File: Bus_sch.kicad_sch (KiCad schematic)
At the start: 9 parts, among them J15 Conn_01x03_Male, J16 Conn_01x20_Male, J17 Conn_01x16_Male, U23 74LS244, U24 74LS373, U25 74LS373, U26 74LS373, U27 74LS245, U28 74LS245

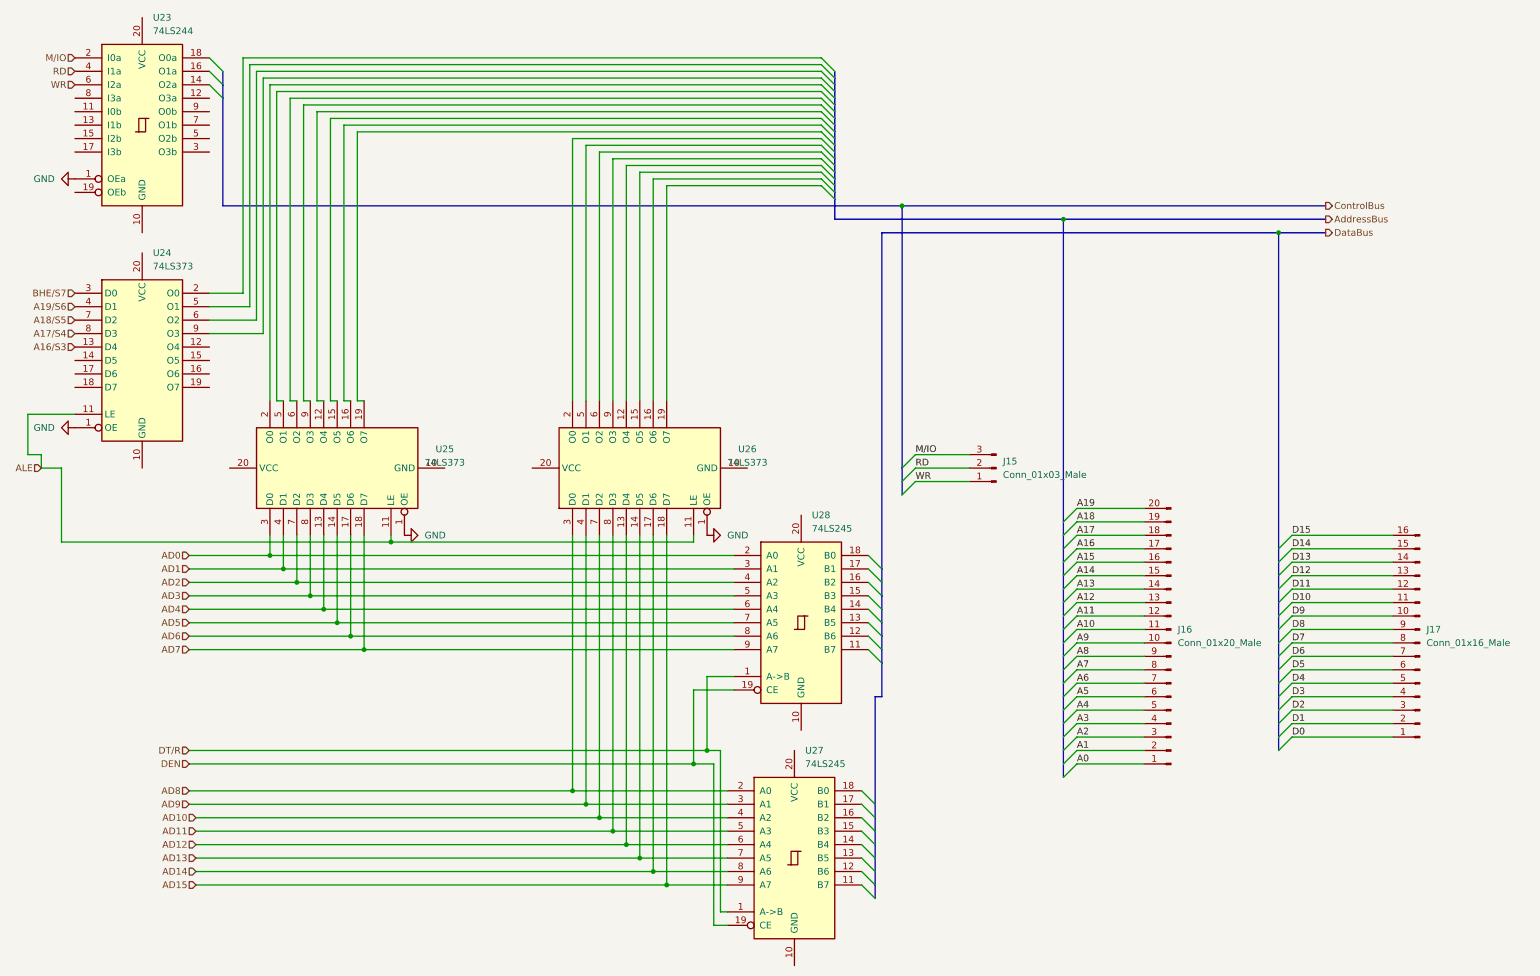
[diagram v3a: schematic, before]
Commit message: Added power and ground to chips
Added power and ground to chips as well as checked and added all labels for pins off of busses
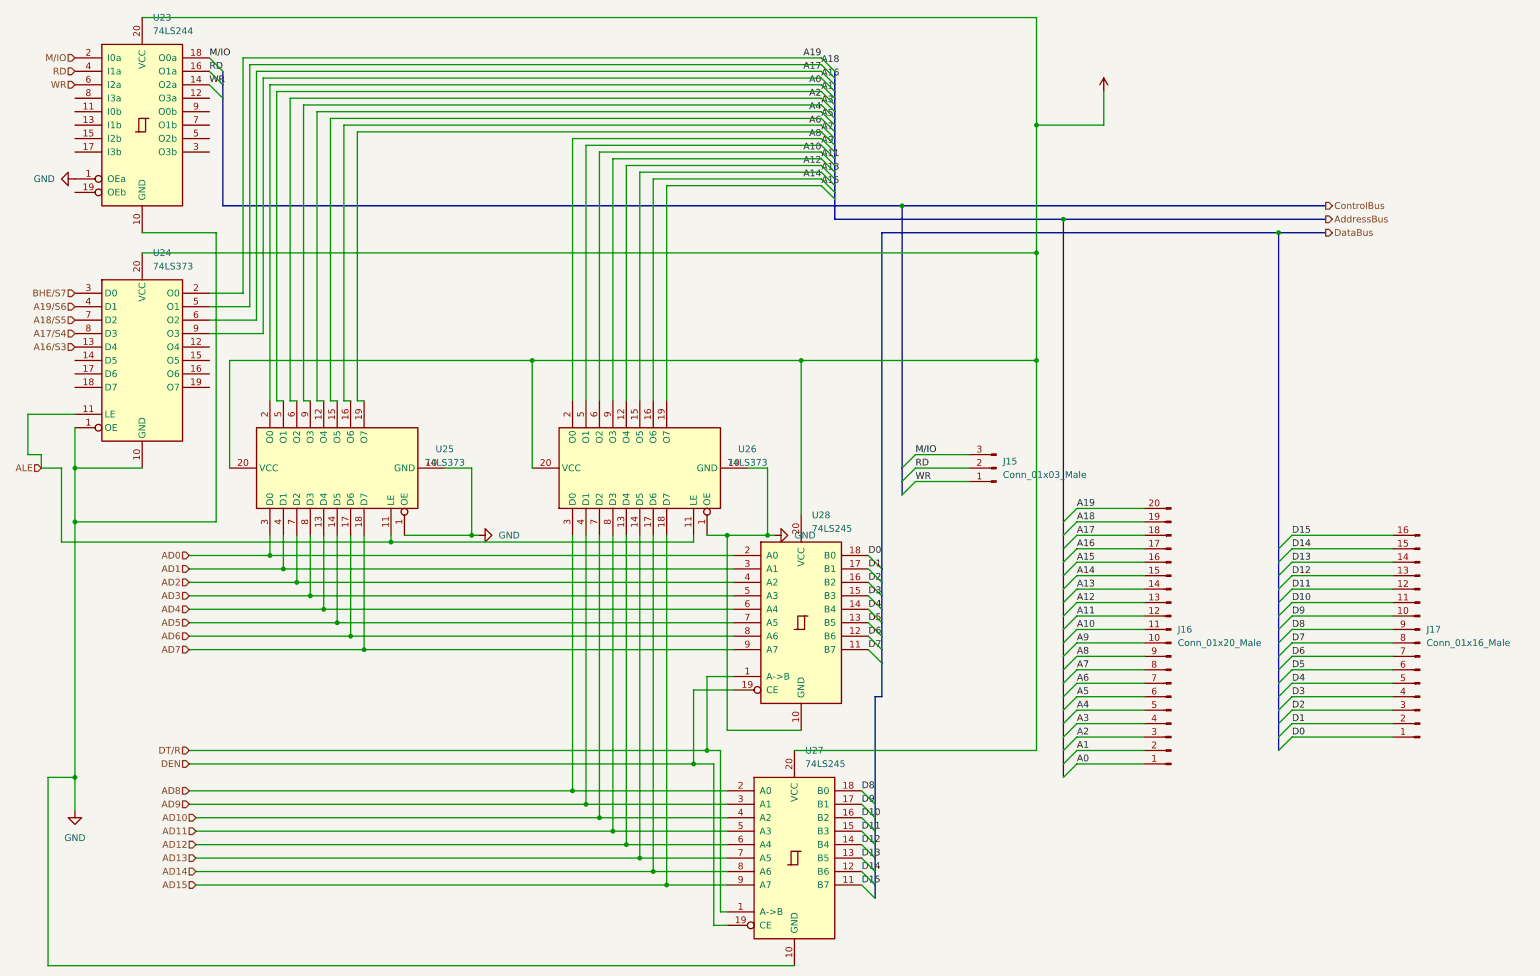
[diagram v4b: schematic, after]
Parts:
- J15, J16, J17: footprint (none) -> Connector:FanPinHeader_1x03_P2.54mm_Vertical
- U23, U24, U25, U26, U27, U28: footprint (none) -> Package_DIP:DIP-20_W7.62mm
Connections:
- net A0: now also U25.2 (O0)
- net A1: now also U25.5 (O1)
- net A10: now also U26.6 (O2)
- net A11: now also U26.9 (O3)
- net A12: now also U26.12 (O4)
- net A13: now also U26.15 (O5)
- net A14: now also U26.16 (O6)
- net A15: now also U26.19 (O7)
- net A16: now also U24.9 (O3)
- net A17: now also U24.6 (O2)
- net A18: now also U24.5 (O1)
- net A19: now also U24.2 (O0)
- net A2: now also U25.6 (O2)
- net A3: now also U25.9 (O3)
- net A4: now also U25.12 (O4)
- net A5: now also U25.15 (O5)
- net A6: now also U25.16 (O6)
- net A7: now also U25.19 (O7)
- net A8: now also U26.2 (O0)
- net A9: now also U26.5 (O1)
- net D0: now also U28.18 (B0)
- net D1: now also U28.17 (B1)
- net D10: now also U27.16 (B2)
- net D11: now also U27.15 (B3)
- net D12: now also U27.14 (B4)
- net D13: now also U27.13 (B5)
- net D14: now also U27.12 (B6)
- net D15: now also U27.11 (B7)
- net D2: now also U28.16 (B2)
- net D3: now also U28.15 (B3)
- net D4: now also U28.14 (B4)
- net D5: now also U28.13 (B5)
- net D6: now also U28.12 (B6)
- net D7: now also U28.11 (B7)
- net D8: now also U27.18 (B0)
- net D9: now also U27.17 (B1)
- net GND: now also U23.10 (GND), U24.10 (GND), U25.10 (GND), U26.10 (GND), U27.10 (GND), U28.10 (GND)
- net M/IO: now also U23.18 (O0a)
- net RD: now also U23.16 (O1a)
- net WR: now also U23.14 (O2a)
- net +5V: now reaches U24.20 (VCC)
- net +5V: now also U23.20 (VCC), U25.20 (VCC), U26.20 (VCC), U27.20 (VCC), U28.20 (VCC)

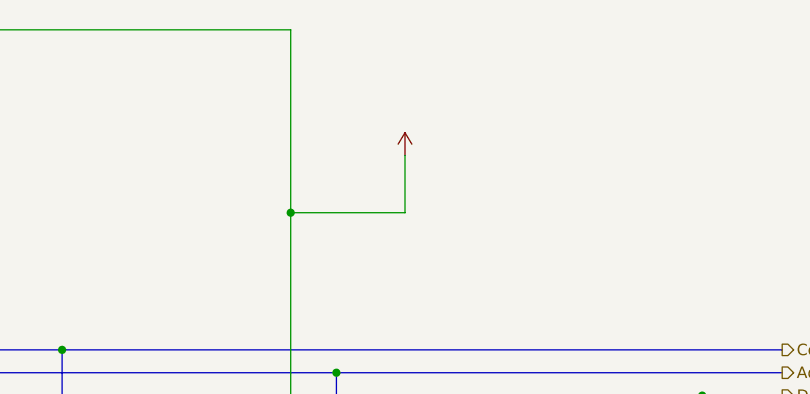
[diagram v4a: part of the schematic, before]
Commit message: Enabled inputs on the max235
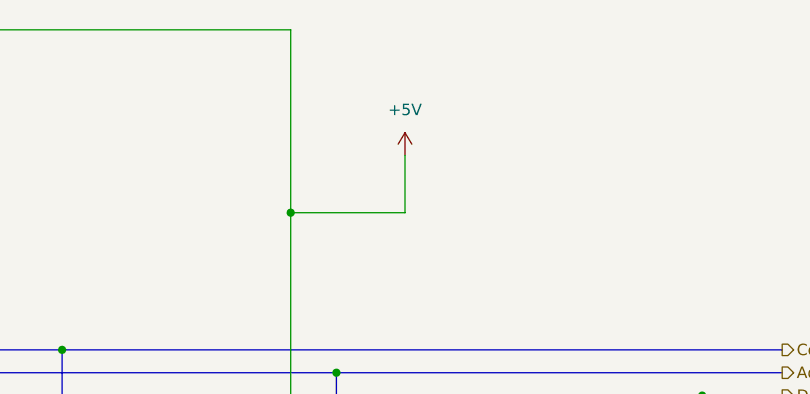
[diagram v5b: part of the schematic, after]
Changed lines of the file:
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@@
       (effects (font (size 1.27 1.27)) hide)
     )
-    (property "Value" "" (id 1) (at 218.44 19.05 0))
+    (property "Value" "+5V" (id 1) (at 218.44 19.05 0))
     (property "Footprint" "" (id 2) (at 218.44 24.13 0)
       (effects (font (size 1.27 1.27)) hide)

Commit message: Updated PCB
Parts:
- J15: value Conn_01x03_Male -> (none); footprint Connector:FanPinHeader_1x03_P2.54mm_Vertical -> (none)
- J16: value Conn_01x20_Male -> (none); footprint Connector:FanPinHeader_1x03_P2.54mm_Vertical -> (none)
- J17: value Conn_01x16_Male -> (none); footprint Connector:FanPinHeader_1x03_P2.54mm_Vertical -> (none)
- U23: value 74LS244 -> (none); footprint Package_DIP:DIP-20_W7.62mm -> (none)
- U24, U25, U26: value 74LS373 -> (none); footprint Package_DIP:DIP-20_W7.62mm -> (none)
- U27, U28: value 74LS245 -> (none); footprint Package_DIP:DIP-20_W7.62mm -> (none)
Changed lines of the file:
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@@
       (effects (font (size 1.27 1.27)) (justify left))
     )
-    (property "Value" "74LS373" (id 1) (at 38.8494 57.15 0)
-      (effects (font (size 1.27 1.27)) (justify left))
-    )
-    (property "Footprint" "Package_DIP:DIP-20_W7.62mm" (id 2) (at 36.83 74.93 0)
+    (property "Value" "" (id 1) (at 38.8494 57.15 0)
+      (effects (font (size 1.27 1.27)) (justify left))
+    )
+    (property "Footprint" "" (id 2) (at 36.83 74.93 0)
       (effects (font (size 1.27 1.27)) hide)
     )
@@
     (in_bom yes) (on_board yes) (fields_autoplaced)
     (property "Reference" "U26" (id 0) (at 151.13 91.6686 90))
-    (property "Value" "74LS373" (id 1) (at 151.13 94.2086 90))
-    (property "Footprint" "Package_DIP:DIP-20_W7.62mm" (id 2) (at 130.81 95.25 0)
+    (property "Value" "" (id 1) (at 151.13 94.2086 90))
+    (property "Footprint" "" (id 2) (at 130.81 95.25 0)
       (effects (font (size 1.27 1.27)) hide)
     )
@@
       (effects (font (size 1.27 1.27)) (justify left))
     )
-    (property "Value" "74LS245" (id 1) (at 163.3094 106.68 0)
-      (effects (font (size 1.27 1.27)) (justify left))
-    )
-    (property "Footprint" "Package_DIP:DIP-20_W7.62mm" (id 2) (at 161.29 124.46 0)
+    (property "Value" "" (id 1) (at 163.3094 106.68 0)
+      (effects (font (size 1.27 1.27)) (justify left))
+    )
+    (property "Footprint" "" (id 2) (at 161.29 124.46 0)
       (effects (font (size 1.27 1.27)) hide)
     )
@@
       (effects (font (size 1.27 1.27)) (justify right))
     )
-    (property "Value" "Conn_01x16_Male" (id 1) (at 279.4 128.2699 0)
-      (effects (font (size 1.27 1.27)) (justify right))
-    )
-    (property "Footprint" "Connector:FanPinHeader_1x03_P2.54mm_Vertical" (id 2) (at 278.13 128.27 0)
+    (property "Value" "" (id 1) (at 279.4 128.2699 0)
+      (effects (font (size 1.27 1.27)) (justify right))
+    )
+    (property "Footprint" "" (id 2) (at 278.13 128.27 0)
       (effects (font (size 1.27 1.27)) hide)
     )
@@
   (symbol (lib_id "power:+5V") (at 218.44 24.13 0) (unit 1)
     (in_bom yes) (on_board yes) (fields_autoplaced)
-    (property "Reference" "#PWR?" (id 0) (at 218.44 27.94 0)
+    (property "Reference" "#PWR0131" (id 0) (at 218.44 27.94 0)
       (effects (font (size 1.27 1.27)) hide)
     )
@@
       (effects (font (size 1.27 1.27)) (justify right))
     )
-    (property "Value" "Conn_01x20_Male" (id 1) (at 232.41 128.2699 0)
-      (effects (font (size 1.27 1.27)) (justify right))
-    )
-    (property "Footprint" "Connector:FanPinHeader_1x03_P2.54mm_Vertical" (id 2) (at 231.14 128.27 0)
+    (property "Value" "" (id 1) (at 232.41 128.2699 0)
+      (effects (font (size 1.27 1.27)) (justify right))
+    )
+    (property "Footprint" "" (id 2) (at 231.14 128.27 0)
       (effects (font (size 1.27 1.27)) hide)
     )
@@
     (in_bom yes) (on_board yes) (fields_autoplaced)
     (property "Reference" "U25" (id 0) (at 93.98 91.6686 90))
-    (property "Value" "74LS373" (id 1) (at 93.98 94.2086 90))
-    (property "Footprint" "Package_DIP:DIP-20_W7.62mm" (id 2) (at 73.66 95.25 0)
+    (property "Value" "" (id 1) (at 93.98 94.2086 90))
+    (property "Footprint" "" (id 2) (at 73.66 95.25 0)
       (effects (font (size 1.27 1.27)) hide)
     )
@@
       (effects (font (size 1.27 1.27)) (justify left))
     )
-    (property "Value" "74LS245" (id 1) (at 162.0394 151.13 0)
-      (effects (font (size 1.27 1.27)) (justify left))
-    )
-    (property "Footprint" "Package_DIP:DIP-20_W7.62mm" (id 2) (at 160.02 168.91 0)
+    (property "Value" "" (id 1) (at 162.0394 151.13 0)
+      (effects (font (size 1.27 1.27)) (justify left))
+    )
+    (property "Footprint" "" (id 2) (at 160.02 168.91 0)
       (effects (font (size 1.27 1.27)) hide)
     )
@@
       (effects (font (size 1.27 1.27)) (justify right))
     )
-    (property "Value" "Conn_01x03_Male" (id 1) (at 199.39 96.5199 0)
-      (effects (font (size 1.27 1.27)) (justify right))
-    )
-    (property "Footprint" "Connector:FanPinHeader_1x03_P2.54mm_Vertical" (id 2) (at 198.12 95.25 0)
+    (property "Value" "" (id 1) (at 199.39 96.5199 0)
+      (effects (font (size 1.27 1.27)) (justify right))
+    )
+    (property "Footprint" "" (id 2) (at 198.12 95.25 0)
       (effects (font (size 1.27 1.27)) hide)
     )
@@
       (effects (font (size 1.27 1.27)) (justify left))
     )
-    (property "Value" "74LS244" (id 1) (at 38.8494 12.7 0)
-      (effects (font (size 1.27 1.27)) (justify left))
-    )
-    (property "Footprint" "Package_DIP:DIP-20_W7.62mm" (id 2) (at 36.83 30.48 0)
-      (effects (font (size 1.27 1.27)) hide)
-    )
+    (property "Value" "" (id 1) (at 38.8494 12.7 0)
+      (effects (font (size 1.27 1.27)) (justify left))
+    )
+    (property "Footprint" "" (id 2) (at 36.83 30.48 0)
+      (effects (font (size 1.27 1.27)) hide)
+    )

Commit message: PCB wiring
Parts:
- J15: value (none) -> Conn_01x03_Male; footprint (none) -> Connector:FanPinHeader_1x03_P2.54mm_Vertical
- J16: value (none) -> Conn_01x20_Male; footprint (none) -> Connector:FanPinHeader_1x03_P2.54mm_Vertical
- J17: value (none) -> Conn_01x16_Male; footprint (none) -> Connector:FanPinHeader_1x03_P2.54mm_Vertical
- U23: value (none) -> 74LS244; footprint (none) -> Package_DIP:DIP-20_W7.62mm
- U24, U25, U26: value (none) -> 74LS373; footprint (none) -> Package_DIP:DIP-20_W7.62mm
- U27, U28: value (none) -> 74LS245; footprint (none) -> Package_DIP:DIP-20_W7.62mm
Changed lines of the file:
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@@
       (effects (font (size 1.27 1.27)) (justify left))
     )
-    (property "Value" "" (id 1) (at 38.8494 57.15 0)
-      (effects (font (size 1.27 1.27)) (justify left))
-    )
-    (property "Footprint" "" (id 2) (at 36.83 74.93 0)
+    (property "Value" "74LS373" (id 1) (at 38.8494 57.15 0)
+      (effects (font (size 1.27 1.27)) (justify left))
+    )
+    (property "Footprint" "Package_DIP:DIP-20_W7.62mm" (id 2) (at 36.83 74.93 0)
       (effects (font (size 1.27 1.27)) hide)
     )
@@
     (in_bom yes) (on_board yes) (fields_autoplaced)
     (property "Reference" "U26" (id 0) (at 151.13 91.6686 90))
-    (property "Value" "" (id 1) (at 151.13 94.2086 90))
-    (property "Footprint" "" (id 2) (at 130.81 95.25 0)
+    (property "Value" "74LS373" (id 1) (at 151.13 94.2086 90))
+    (property "Footprint" "Package_DIP:DIP-20_W7.62mm" (id 2) (at 130.81 95.25 0)
       (effects (font (size 1.27 1.27)) hide)
     )
@@
       (effects (font (size 1.27 1.27)) (justify left))
     )
-    (property "Value" "" (id 1) (at 163.3094 106.68 0)
-      (effects (font (size 1.27 1.27)) (justify left))
-    )
-    (property "Footprint" "" (id 2) (at 161.29 124.46 0)
+    (property "Value" "74LS245" (id 1) (at 163.3094 106.68 0)
+      (effects (font (size 1.27 1.27)) (justify left))
+    )
+    (property "Footprint" "Package_DIP:DIP-20_W7.62mm" (id 2) (at 161.29 124.46 0)
       (effects (font (size 1.27 1.27)) hide)
     )
@@
       (effects (font (size 1.27 1.27)) (justify right))
     )
-    (property "Value" "" (id 1) (at 279.4 128.2699 0)
-      (effects (font (size 1.27 1.27)) (justify right))
-    )
-    (property "Footprint" "" (id 2) (at 278.13 128.27 0)
+    (property "Value" "Conn_01x16_Male" (id 1) (at 279.4 128.2699 0)
+      (effects (font (size 1.27 1.27)) (justify right))
+    )
+    (property "Footprint" "Connector:FanPinHeader_1x03_P2.54mm_Vertical" (id 2) (at 278.13 128.27 0)
       (effects (font (size 1.27 1.27)) hide)
     )
@@
       (effects (font (size 1.27 1.27)) (justify right))
     )
-    (property "Value" "" (id 1) (at 232.41 128.2699 0)
-      (effects (font (size 1.27 1.27)) (justify right))
-    )
-    (property "Footprint" "" (id 2) (at 231.14 128.27 0)
+    (property "Value" "Conn_01x20_Male" (id 1) (at 232.41 128.2699 0)
+      (effects (font (size 1.27 1.27)) (justify right))
+    )
+    (property "Footprint" "Connector:FanPinHeader_1x03_P2.54mm_Vertical" (id 2) (at 231.14 128.27 0)
       (effects (font (size 1.27 1.27)) hide)
     )
@@
     (in_bom yes) (on_board yes) (fields_autoplaced)
     (property "Reference" "U25" (id 0) (at 93.98 91.6686 90))
-    (property "Value" "" (id 1) (at 93.98 94.2086 90))
-    (property "Footprint" "" (id 2) (at 73.66 95.25 0)
+    (property "Value" "74LS373" (id 1) (at 93.98 94.2086 90))
+    (property "Footprint" "Package_DIP:DIP-20_W7.62mm" (id 2) (at 73.66 95.25 0)
       (effects (font (size 1.27 1.27)) hide)
     )
@@
       (effects (font (size 1.27 1.27)) (justify left))
     )
-    (property "Value" "" (id 1) (at 162.0394 151.13 0)
-      (effects (font (size 1.27 1.27)) (justify left))
-    )
-    (property "Footprint" "" (id 2) (at 160.02 168.91 0)
+    (property "Value" "74LS245" (id 1) (at 162.0394 151.13 0)
+      (effects (font (size 1.27 1.27)) (justify left))
+    )
+    (property "Footprint" "Package_DIP:DIP-20_W7.62mm" (id 2) (at 160.02 168.91 0)
       (effects (font (size 1.27 1.27)) hide)
     )
@@
       (effects (font (size 1.27 1.27)) (justify right))
     )
-    (property "Value" "" (id 1) (at 199.39 96.5199 0)
-      (effects (font (size 1.27 1.27)) (justify right))
-    )
-    (property "Footprint" "" (id 2) (at 198.12 95.25 0)
+    (property "Value" "Conn_01x03_Male" (id 1) (at 199.39 96.5199 0)
+      (effects (font (size 1.27 1.27)) (justify right))
+    )
+    (property "Footprint" "Connector:FanPinHeader_1x03_P2.54mm_Vertical" (id 2) (at 198.12 95.25 0)
       (effects (font (size 1.27 1.27)) hide)
     )
@@
       (effects (font (size 1.27 1.27)) (justify left))
     )
-    (property "Value" "" (id 1) (at 38.8494 12.7 0)
-      (effects (font (size 1.27 1.27)) (justify left))
-    )
-    (property "Footprint" "" (id 2) (at 36.83 30.48 0)
-      (effects (font (size 1.27 1.27)) hide)
-    )
+    (property "Value" "74LS244" (id 1) (at 38.8494 12.7 0)
+      (effects (font (size 1.27 1.27)) (justify left))
+    )
+    (property "Footprint" "Package_DIP:DIP-20_W7.62mm" (id 2) (at 36.83 30.48 0)
+      (effects (font (size 1.27 1.27)) hide)
+    )

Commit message: pcb wiring
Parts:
- J16, J17: footprint Connector:FanPinHeader_1x03_P2.54mm_Vertical -> (none)
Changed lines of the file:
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@@
       (effects (font (size 1.27 1.27)) (justify right))
     )
-    (property "Footprint" "Connector:FanPinHeader_1x03_P2.54mm_Vertical" (id 2) (at 278.13 128.27 0)
+    (property "Footprint" "" (id 2) (at 278.13 128.27 0)
       (effects (font (size 1.27 1.27)) hide)
     )
@@
       (effects (font (size 1.27 1.27)) (justify right))
     )
-    (property "Footprint" "Connector:FanPinHeader_1x03_P2.54mm_Vertical" (id 2) (at 231.14 128.27 0)
+    (property "Footprint" "" (id 2) (at 231.14 128.27 0)
       (effects (font (size 1.27 1.27)) hide)
     )
